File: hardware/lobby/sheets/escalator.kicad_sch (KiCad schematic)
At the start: 2 parts

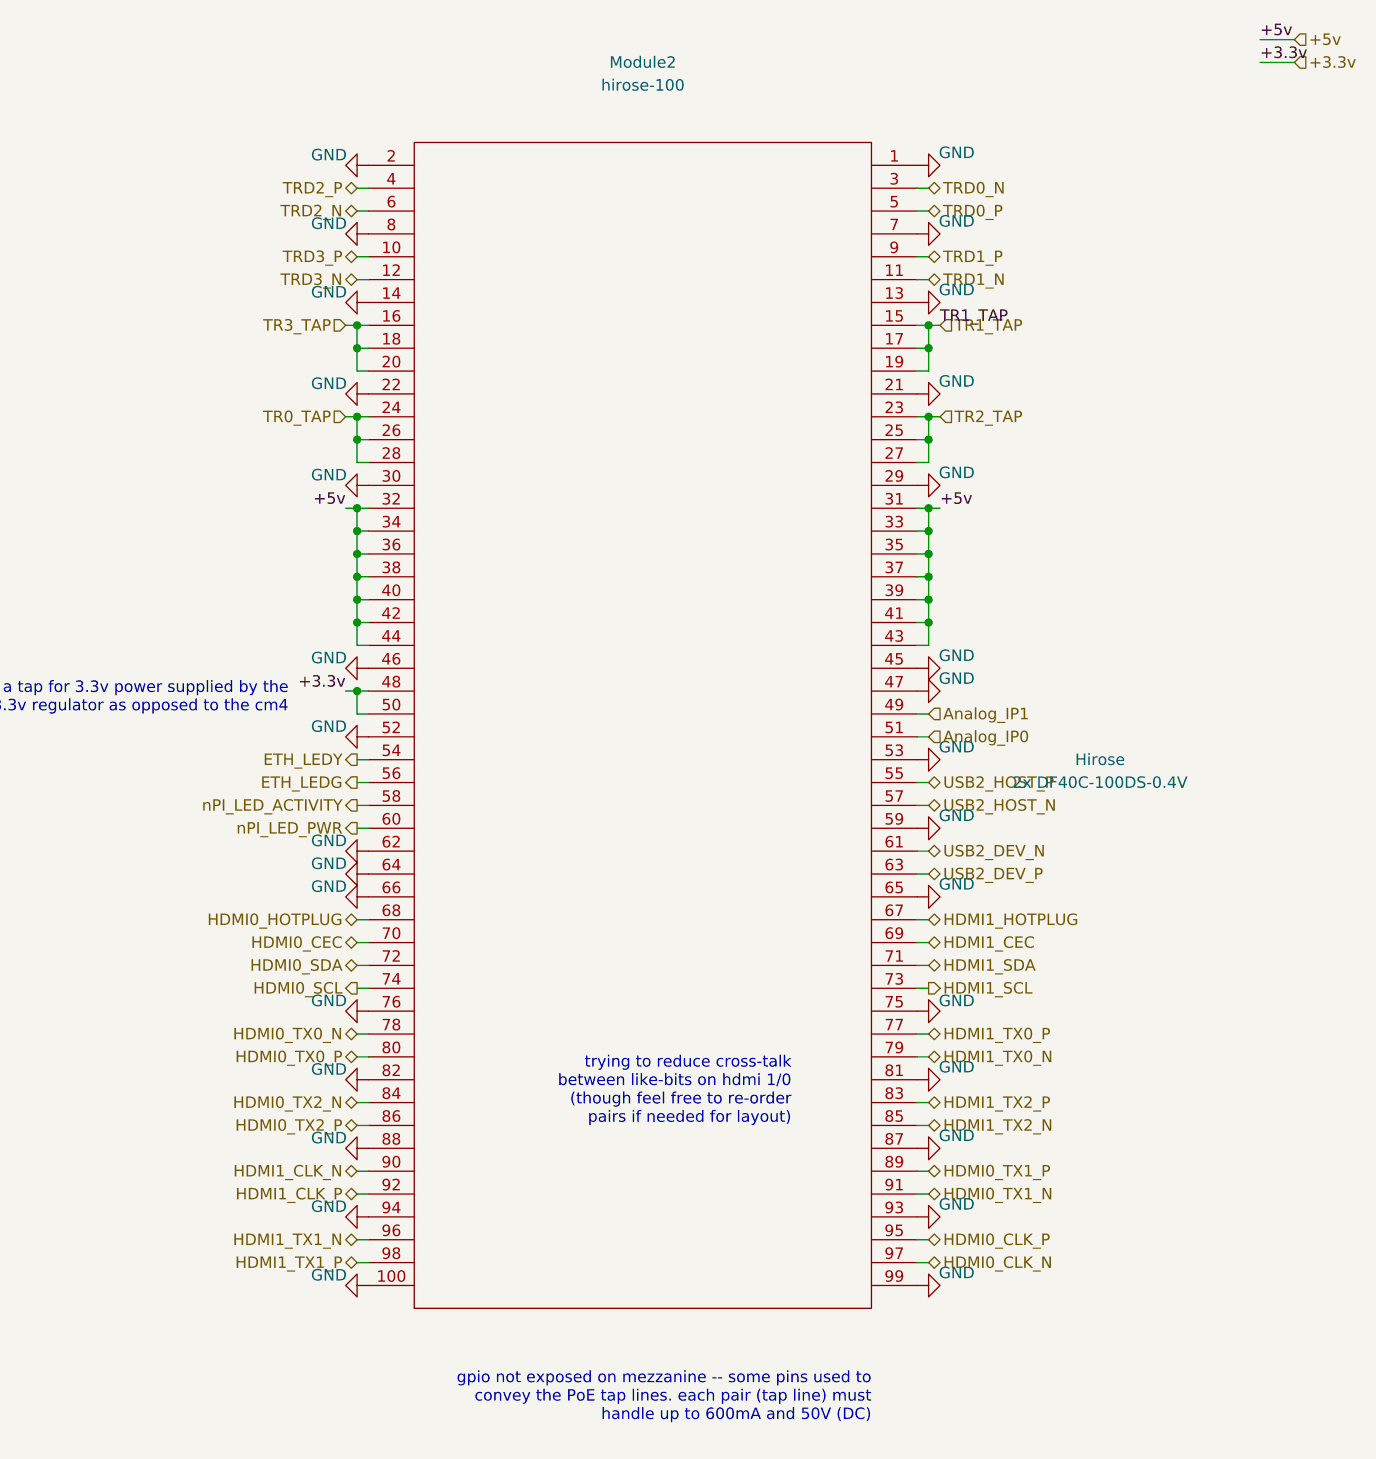
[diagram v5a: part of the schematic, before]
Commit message: mirror lobby mezzanine connector
fixing a big whoops
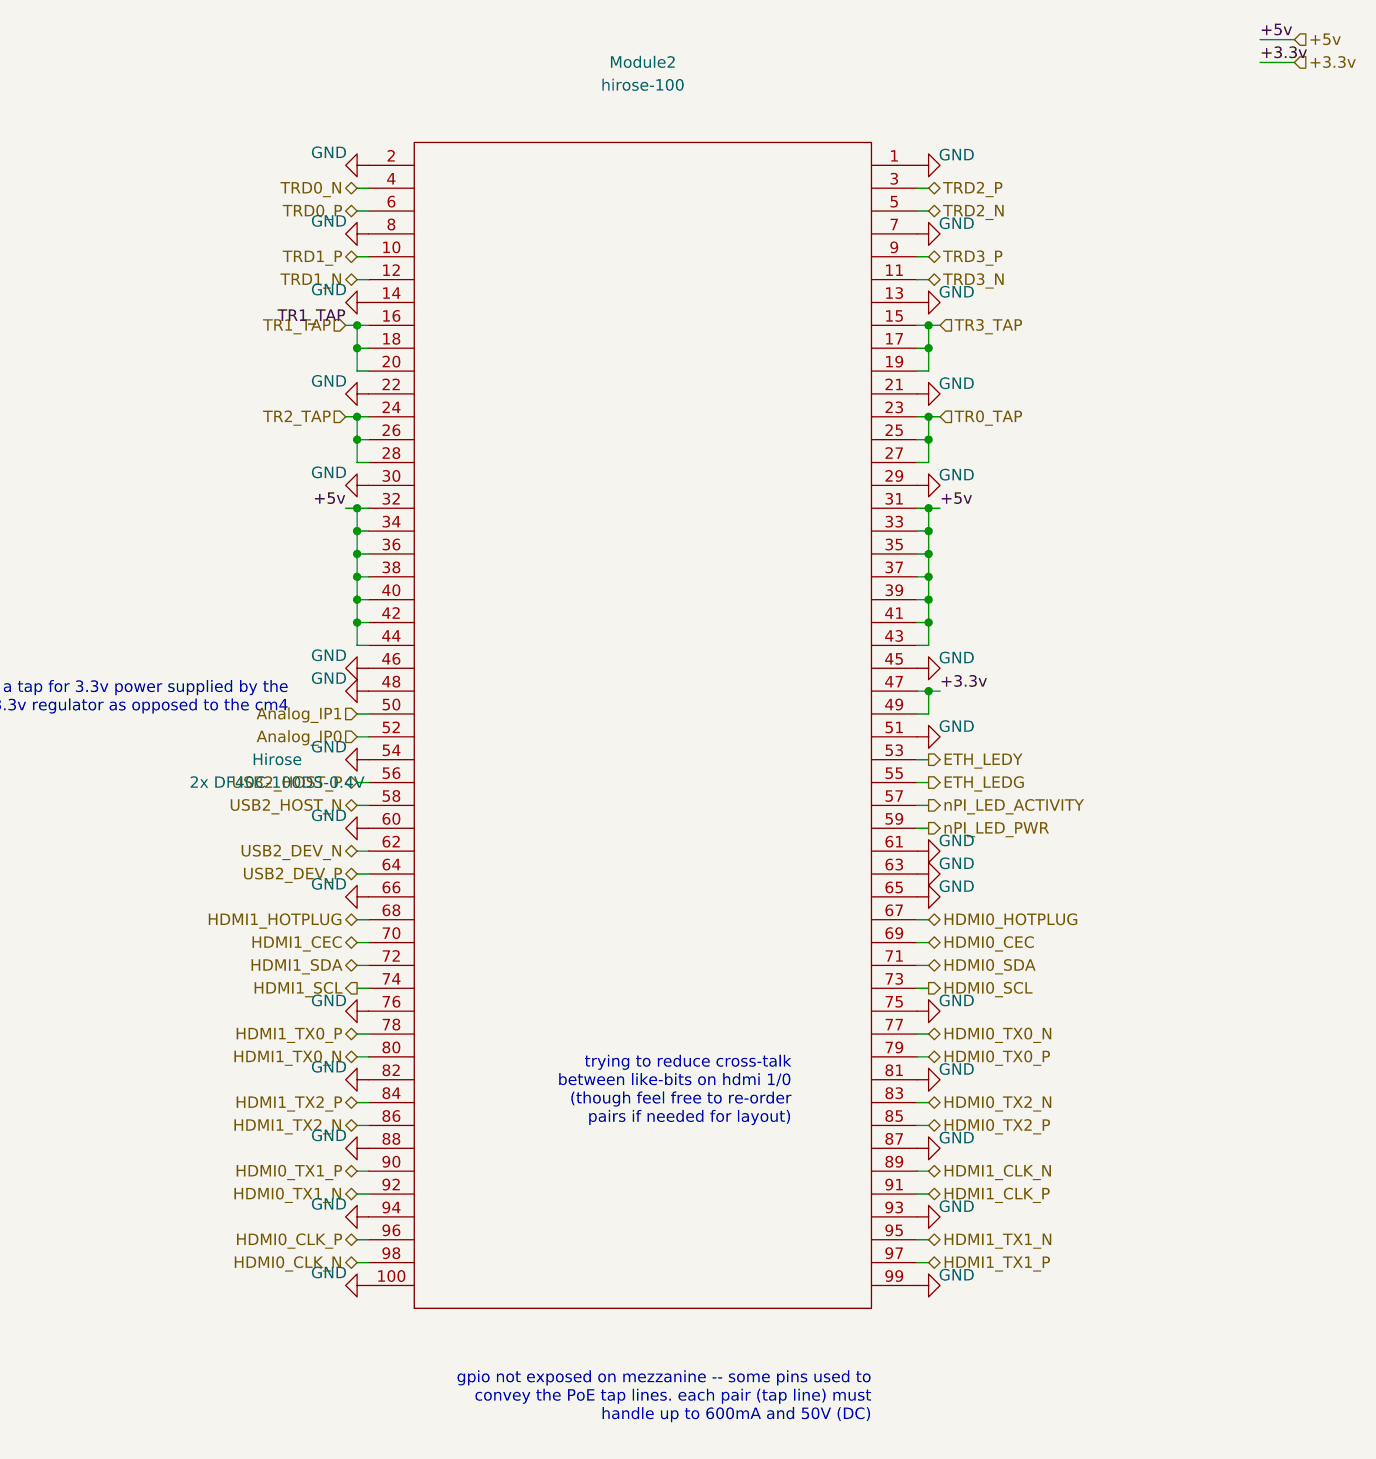
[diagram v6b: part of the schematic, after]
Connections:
- net +3.3v: now also Module2.47, Module2.49; no longer Module2.48, Module2.50
- net Analog_IP0: now also Module2.52; no longer Module2.51
- net Analog_IP1: now also Module2.50; no longer Module2.49
- net ETH_LEDG: now also Module2.55; no longer Module2.56
- net ETH_LEDY: now also Module2.53; no longer Module2.54
- net GND: now also Module2.48, Module2.51, Module2.54, Module2.60, Module2.61, Module2.63; no longer Module2.47, Module2.52, Module2.53, Module2.59, Module2.62, Module2.64
- net HDMI0_CEC: now also Module2.69; no longer Module2.70
- net HDMI0_CLK_N: now also Module2.98; no longer Module2.97
- net HDMI0_CLK_P: now also Module2.96; no longer Module2.95
- net HDMI0_HOTPLUG: now also Module2.67; no longer Module2.68
- net HDMI0_SCL: now also Module2.73; no longer Module2.74
- net HDMI0_SDA: now also Module2.71; no longer Module2.72
- net HDMI0_TX0_N: now also Module2.77; no longer Module2.78
- net HDMI0_TX0_P: now also Module2.79; no longer Module2.80
- net HDMI0_TX1_N: now also Module2.92; no longer Module2.91
- net HDMI0_TX1_P: now also Module2.90; no longer Module2.89
- net HDMI0_TX2_N: now also Module2.83; no longer Module2.84
- net HDMI0_TX2_P: now also Module2.85; no longer Module2.86
- net HDMI1_CEC: now also Module2.70; no longer Module2.69
- net HDMI1_CLK_N: now also Module2.89; no longer Module2.90
- net HDMI1_CLK_P: now also Module2.91; no longer Module2.92
- net HDMI1_HOTPLUG: now also Module2.68; no longer Module2.67
- net HDMI1_SCL: now also Module2.74; no longer Module2.73
- net HDMI1_SDA: now also Module2.72; no longer Module2.71
- net HDMI1_TX0_N: now also Module2.80; no longer Module2.79
- net HDMI1_TX0_P: now also Module2.78; no longer Module2.77
- net HDMI1_TX1_N: now also Module2.95; no longer Module2.96
- net HDMI1_TX1_P: now also Module2.97; no longer Module2.98
- net HDMI1_TX2_N: now also Module2.86; no longer Module2.85
- net HDMI1_TX2_P: now also Module2.84; no longer Module2.83
- net TR0_TAP: now also Module2.23, Module2.25, Module2.27; no longer Module2.24, Module2.26, Module2.28
- net TR1_TAP: now also Module2.16, Module2.18, Module2.20; no longer Module2.15, Module2.17, Module2.19
- net TR2_TAP: now also Module2.24, Module2.26, Module2.28; no longer Module2.23, Module2.25, Module2.27
- net TR3_TAP: now also Module2.15, Module2.17, Module2.19; no longer Module2.16, Module2.18, Module2.20
- net TRD0_N: now also Module2.4; no longer Module2.3
- net TRD0_P: now also Module2.6; no longer Module2.5
- net TRD1_N: now also Module2.12; no longer Module2.11
- net TRD1_P: now also Module2.10; no longer Module2.9
- net TRD2_N: now also Module2.5; no longer Module2.6
- net TRD2_P: now also Module2.3; no longer Module2.4
- net TRD3_N: now also Module2.11; no longer Module2.12
- net TRD3_P: now also Module2.9; no longer Module2.10
- net USB2_DEV_N: now also Module2.62; no longer Module2.61
- net USB2_DEV_P: now also Module2.64; no longer Module2.63
- net USB2_HOST_N: now also Module2.58; no longer Module2.57
- net USB2_HOST_P: now also Module2.56; no longer Module2.55
- net nPI_LED_ACTIVITY: now also Module2.57; no longer Module2.58
- net nPI_LED_PWR: now also Module2.59; no longer Module2.60

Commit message: change lobby hirose connectors to the DS variant
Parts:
- Module2, Module3: footprint cm4crypto:DF40C-100DP-0.4V(51) -> cm4crypto:DF40C-100DS-0.4V(51)
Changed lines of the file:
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@@
     (property "Reference" "Module2" (id 0) (at 85.09 19.05 0))
     (property "Value" "hirose-100" (id 1) (at 85.09 21.59 0))
-    (property "Footprint" "cm4crypto:DF40C-100DP-0.4V(51)" (id 2) (at 95.25 212.09 0)
+    (property "Footprint" "cm4crypto:DF40C-100DS-0.4V(51)" (id 2) (at 95.25 212.09 0)
       (effects (font (size 1.27 1.27)) hide)
     )
@@
     (property "Reference" "Module3" (id 0) (at 213.36 19.05 0))
     (property "Value" "hirose-100" (id 1) (at 213.36 21.59 0))
-    (property "Footprint" "cm4crypto:DF40C-100DP-0.4V(51)" (id 2) (at 223.52 212.09 0)
+    (property "Footprint" "cm4crypto:DF40C-100DS-0.4V(51)" (id 2) (at 223.52 212.09 0)
       (effects (font (size 1.27 1.27)) hide)
     )
